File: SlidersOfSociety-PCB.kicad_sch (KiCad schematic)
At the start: 13 parts, among them J1 Conn_01x08_Male, J2 6P4C, J3 6P4C, SW1 219-4MST, SW2 limit switch, U1 PIC18F25K83-I/SO, U2 DRV8871DDA, U3 MCP2561-E-SN

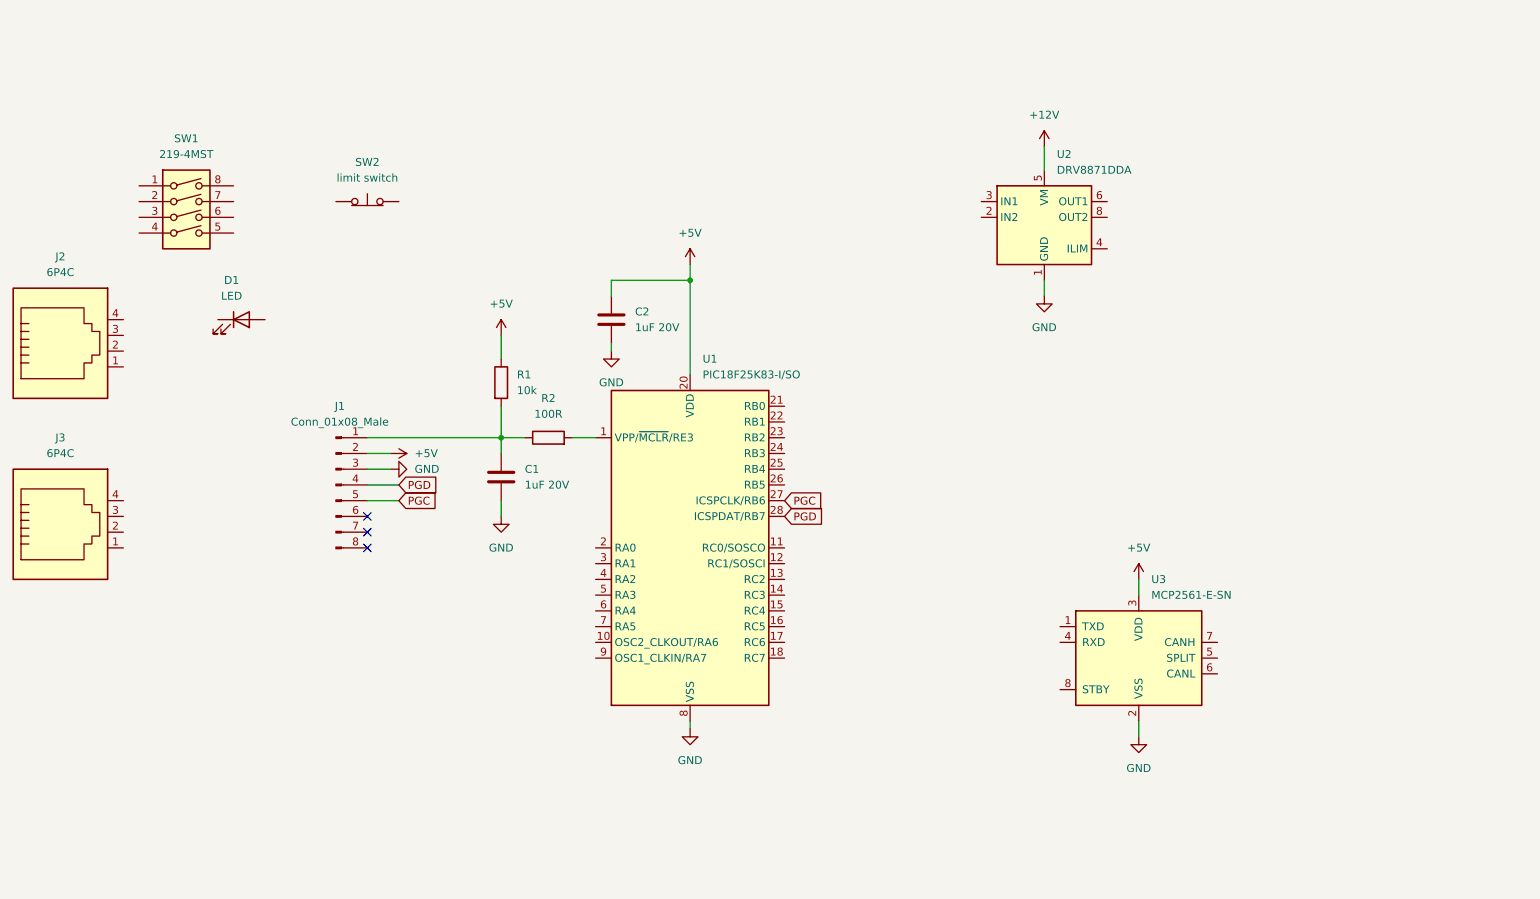
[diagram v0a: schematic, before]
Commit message: bump to kicad 9.0.2
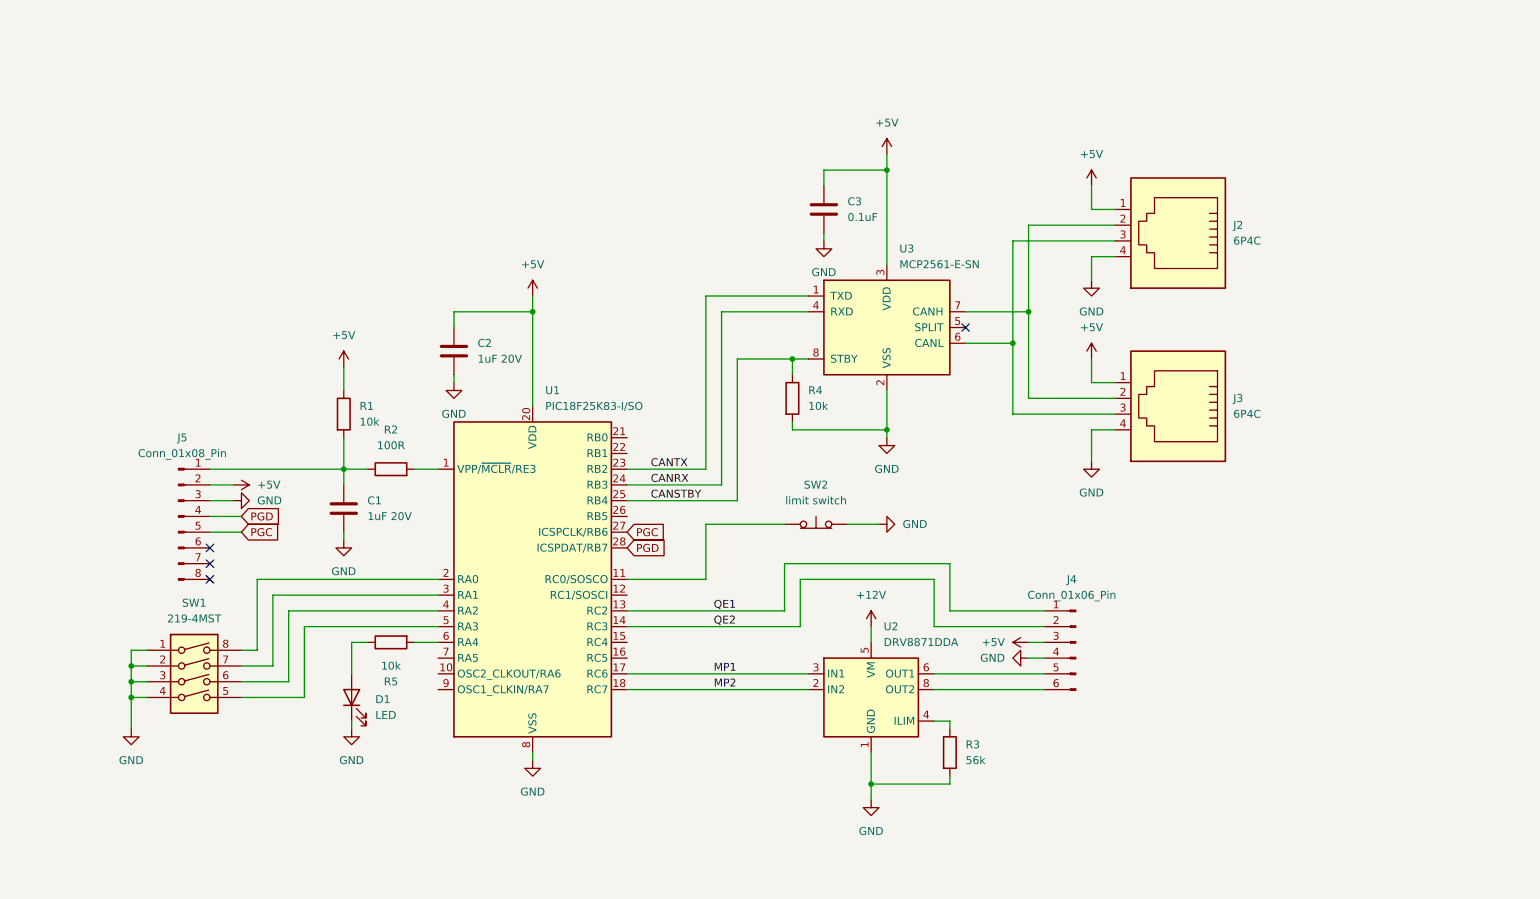
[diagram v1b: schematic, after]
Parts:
- removed J1: Conn_01x08_Male, Connector_PinHeader_2.54mm:PinHeader_1x08_P2.54mm_Vertical, symbol Connector:Conn_01x08_Male
- added C3: 0.1uF, symbol Device:C
- added J4: Conn_01x06_Pin, Connector_PinHeader_2.54mm:PinHeader_1x06_P2.54mm_Horizontal, symbol Connector:Conn_01x06_Pin
- added J5: Conn_01x08_Pin, Connector_PinHeader_2.54mm:PinHeader_1x08_P2.54mm_Vertical, symbol Connector:Conn_01x08_Pin
- added R3: 56k, Resistor_THT:R_Axial_DIN0207_L6.3mm_D2.5mm_P7.62mm_Horizontal, symbol Device:R
- added R4, R5: 10k, Resistor_THT:R_Axial_DIN0207_L6.3mm_D2.5mm_P7.62mm_Horizontal, symbol Device:R
- R1, R2: footprint (none) -> Resistor_THT:R_Axial_DIN0207_L6.3mm_D2.5mm_P7.62mm_Horizontal
- SW2: footprint (none) -> Connector_PinHeader_2.54mm:PinHeader_1x02_P2.54mm_Horizontal
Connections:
- net +5V: now also J2.1, J3.1, C3.1, J4.3 (Pin_3), J5.2 (Pin_2)
- net GND: now also D1.1 (K), J2.4, J3.4, SW1.1, SW1.2, SW1.3, SW1.4, SW2.2 (B), C3.2, J4.4 (Pin_4), J5.3 (Pin_3), R3.2, R4.2
- net PGC: now also J5.5 (Pin_5)
- net PGD: now also J5.4 (Pin_4)
- net at C1.1, R1.2, R2.1: now also J5.1 (Pin_1)
- net at SW2.1 (A): now also U1.11 (RC0/SOSCO)
- net MP2: now reaches U2.2 (IN2)
- net MP2: now also U1.18 (RC7)
- net MP1: now reaches U2.3 (IN1)
- net MP1: now also U1.17 (RC6)
- net at U2.4 (ILIM): now also R3.1
- net at U2.6 (OUT1): now also J4.5 (Pin_5)
- net at U2.8 (OUT2): now also J4.6 (Pin_6)
- net CANTX: now reaches U3.1 (TXD)
- net CANTX: now also U1.23 (RB2)
- net CANRX: now reaches U3.4 (RXD)
- net CANRX: now also U1.24 (RB3)
- net at U3.6 (CANL): now also J2.3, J3.3
- net at U3.7 (CANH): now also J2.2, J3.2
- net CANSTBY: now reaches U3.8 (STBY)
- net CANSTBY: now also U1.25 (RB4), R4.1
- net at D1.2 (A): now also R5.1
- net QE1: now reaches U1.13 (RC2)
- net QE1: now also J4.1 (Pin_1)
- net QE2: now reaches U1.14 (RC3)
- net QE2: now also J4.2 (Pin_2)
- net at U1.2 (RA0): now also SW1.8
- net at U1.3 (RA1): now also SW1.7
- net at U1.4 (RA2): now also SW1.6
- net at U1.5 (RA3): now also SW1.5
- net at U1.6 (RA4): now also R5.2
- no-connect marks 3 -> 4
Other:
- company: (none) -> OE1KHZ
- title: (none) -> SlidersOfSociety-PCB
- moved on the sheet: C1, C2, D1, J2, J3, R1, R2, SW1, SW2, U1, U2, U3

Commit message: add custom drc
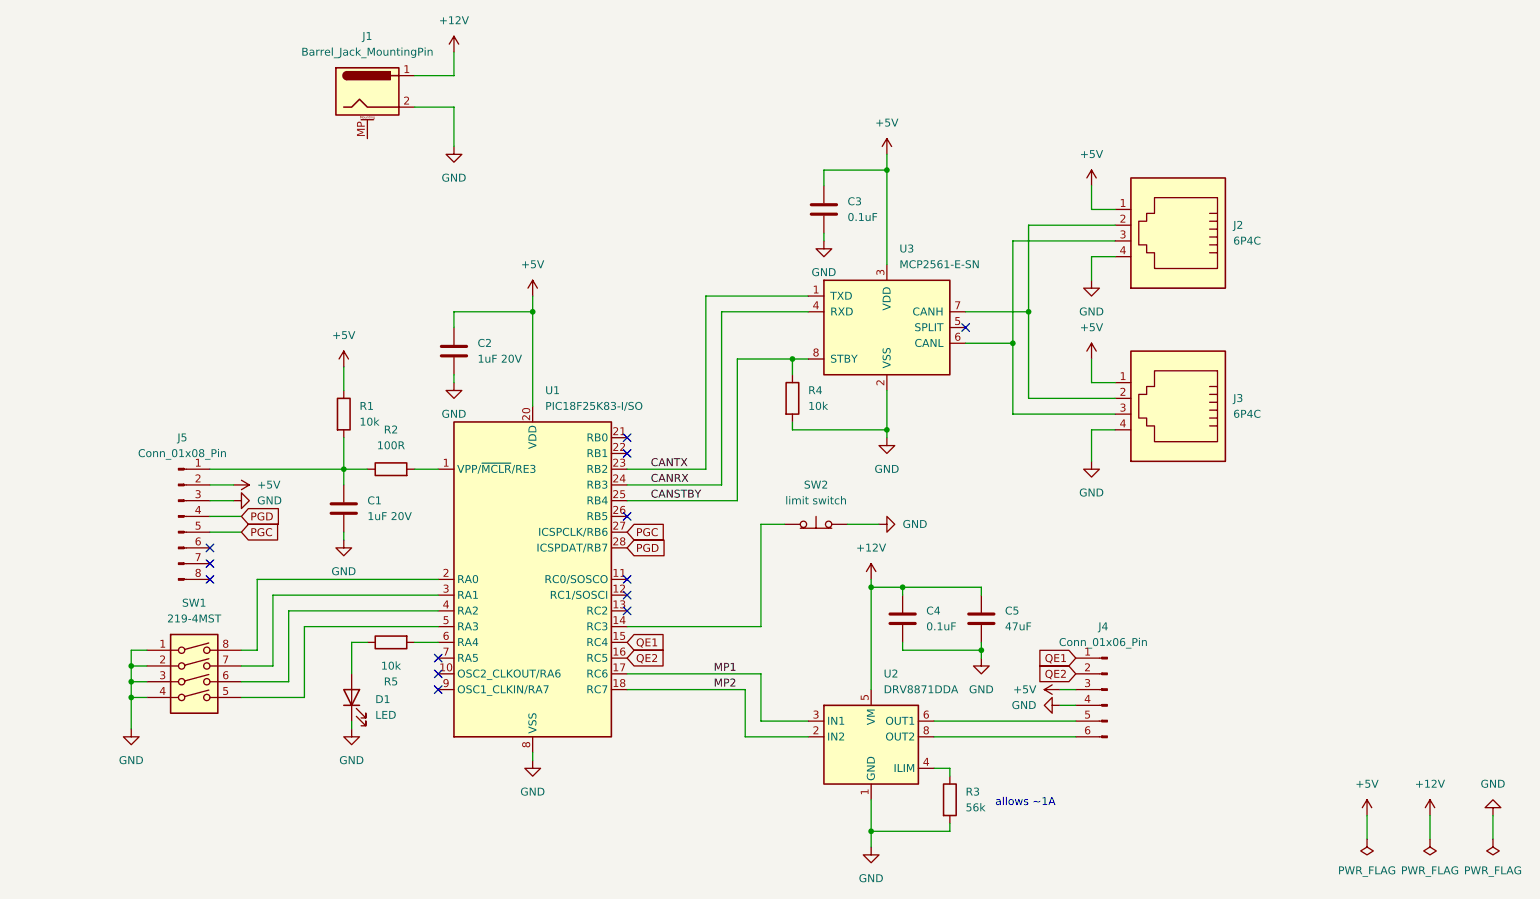
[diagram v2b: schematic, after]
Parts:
- added C4: 0.1uF, Capacitor_SMD:C_0805_2012Metric_Pad1.18x1.45mm_HandSolder, symbol Device:C
- added C5: 47uF, Capacitor_THT:C_Radial_D10.0mm_H12.5mm_P5.00mm, symbol Device:C
- added J1: Barrel_Jack_MountingPin, Connector_BarrelJack:BarrelJack_Horizontal, symbol Connector:Barrel_Jack_MountingPin
- C1, C2: footprint (none) -> Capacitor_SMD:C_0805_2012Metric_Pad1.18x1.45mm_HandSolder; MANUFACTURER_PART_NUMBER (none) -> CL21B105KBFNNNE
- C3: footprint (none) -> Capacitor_SMD:C_0805_2012Metric_Pad1.18x1.45mm_HandSolder; MANUFACTURER_PART_NUMBER (none) -> CC0805KRX7R9BB104
- J2, J3: MANUFACTURER_PART_NUMBER (none) -> MTJ-642BX2
- R1, R2, R4, R5: footprint Resistor_THT:R_Axial_DIN0207_L6.3mm_D2.5mm_P7.62mm_Horizontal -> Resistor_SMD:R_0805_2012Metric_Pad1.20x1.40mm_HandSolder
- SW1: MANUFACTURER_PART_NUMBER (none) -> 219-4MST
- U1: MANUFACTURER_PART_NUMBER (none) -> PIC18F25K83-I/SO
- U2: MANUFACTURER_PART_NUMBER (none) -> DRV8871DDAR
- U3: MANUFACTURER_PART_NUMBER (none) -> MCP2561T-E/SN
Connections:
- net +12V: now also C4.1, C5.1, J1.1
- net GND: now also C4.2, C5.2, J1.2
- net QE1: now also U1.15 (RC4); no longer U1.13 (RC2)
- net QE2: now also U1.16 (RC5); no longer U1.14 (RC3)
- net at SW2.1 (A): now also U1.14 (RC3); no longer U1.11 (RC0/SOSCO)
- no-connect marks 4 -> 13
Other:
- note added: "allows ~1A"
- moved on the sheet: J4, R3, U2

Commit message: finish pcb layout v0.2
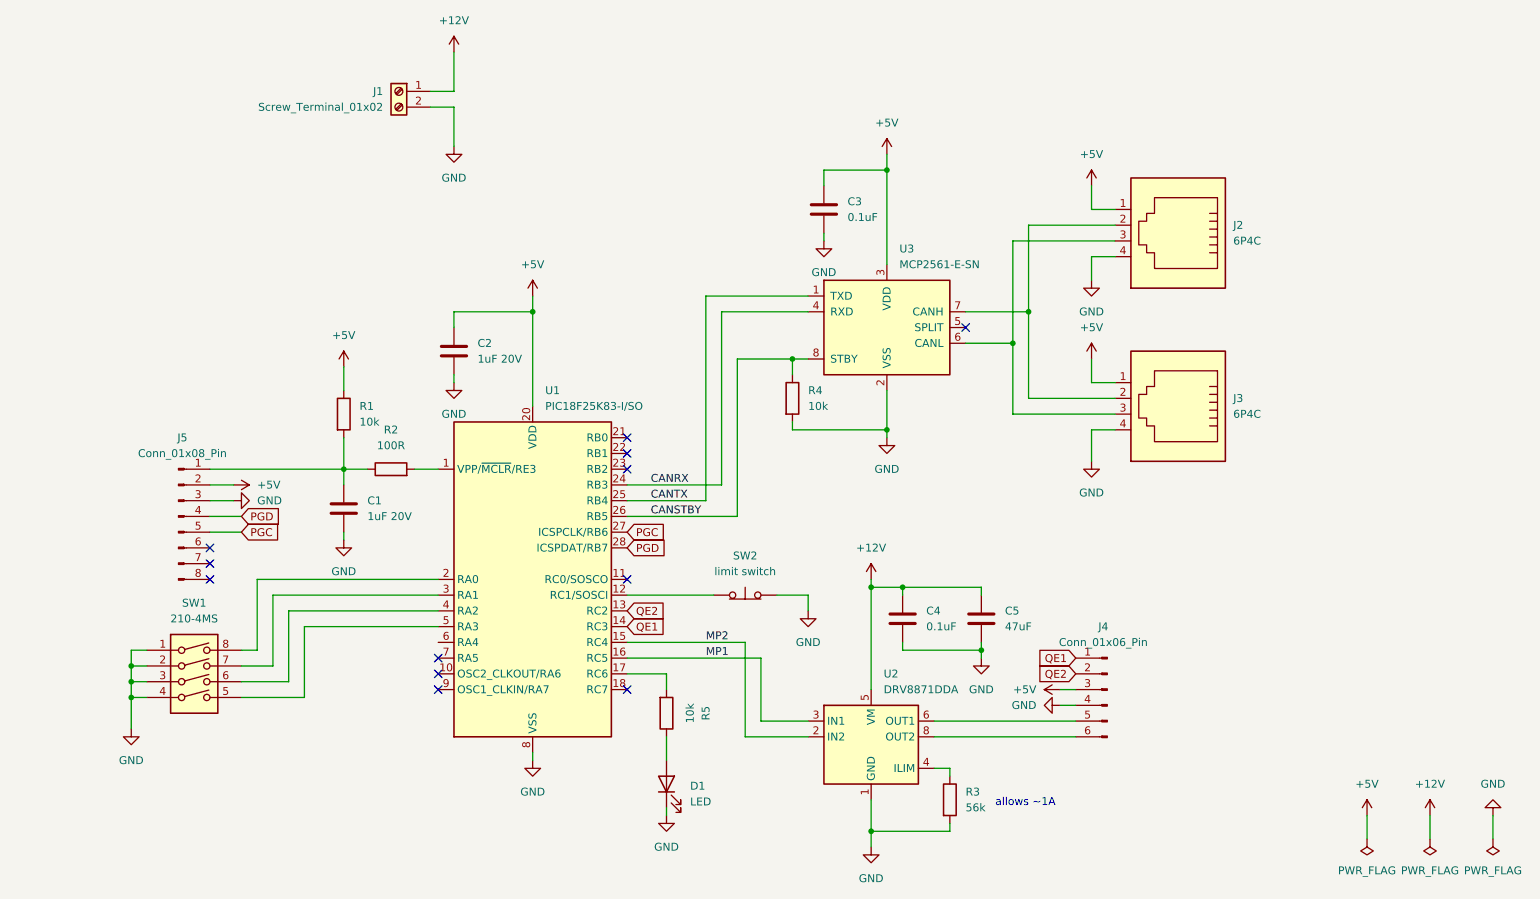
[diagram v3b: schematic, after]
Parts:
- removed J1: Barrel_Jack_MountingPin, Connector_BarrelJack:BarrelJack_Horizontal, symbol Connector:Barrel_Jack_MountingPin
- added J1: Screw_Terminal_01x02, TerminalBlock:TerminalBlock_MaiXu_MX126-5.0-02P_1x02_P5.00mm, symbol Connector:Screw_Terminal_01x02
- J4: footprint Connector_PinHeader_2.54mm:PinHeader_1x06_P2.54mm_Horizontal -> Connector_PinHeader_2.54mm:PinHeader_1x06_P2.54mm_Vertical
- R1, R4, R5: MANUFACTURER_PART_NUMBER (none) -> CRCW080510K0FKEA
- R2: MANUFACTURER_PART_NUMBER (none) -> RC0805FR-07100RL
- R3: footprint Resistor_THT:R_Axial_DIN0207_L6.3mm_D2.5mm_P7.62mm_Horizontal -> Resistor_SMD:R_0805_2012Metric_Pad1.20x1.40mm_HandSolder; MANUFACTURER_PART_NUMBER (none) -> RC0805FR-0756KL
- SW1: value 219-4MST -> 210-4MS; footprint Button_Switch_SMD:SW_DIP_SPSTx04_Slide_6.7x11.72mm_W8.61mm_P2.54mm_LowProfile -> Button_Switch_THT:SW_DIP_SPSTx04_Slide_6.7x11.72mm_W7.62mm_P2.54mm_LowProfile
- SW2: footprint Connector_PinHeader_2.54mm:PinHeader_1x02_P2.54mm_Horizontal -> Connector_JST:JST_XH_B2B-XH-A_1x02_P2.50mm_Vertical
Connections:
- net +12V: now also J1.1 (Pin_1)
- net CANSTBY: now also U1.26 (RB5); no longer U1.25 (RB4)
- net CANTX: now also U1.25 (RB4); no longer U1.23 (RB2)
- net GND: now also J1.2 (Pin_2)
- net MP1: now also U1.16 (RC5); no longer U1.17 (RC6)
- net MP2: now also U1.15 (RC4); no longer U1.18 (RC7)
- net QE1: now also U1.14 (RC3); no longer U1.15 (RC4)
- net QE2: now also U1.13 (RC2); no longer U1.16 (RC5)
- net at SW2.1 (A): now also U1.12 (RC1/SOSCI); no longer U1.14 (RC3)
- net at R5.2: now also U1.17 (RC6); no longer U1.6 (RA4)
- no-connect marks 13 -> 12
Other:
- moved on the sheet: D1, R5, SW2
